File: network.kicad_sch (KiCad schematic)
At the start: 65 parts, among them J1 1840888-1, Q1 BSS138, Q2 BSS138, Q3 BSS138, U2 DP83867IRPAPR, Y1 ECS-2520MV-xxx-xx

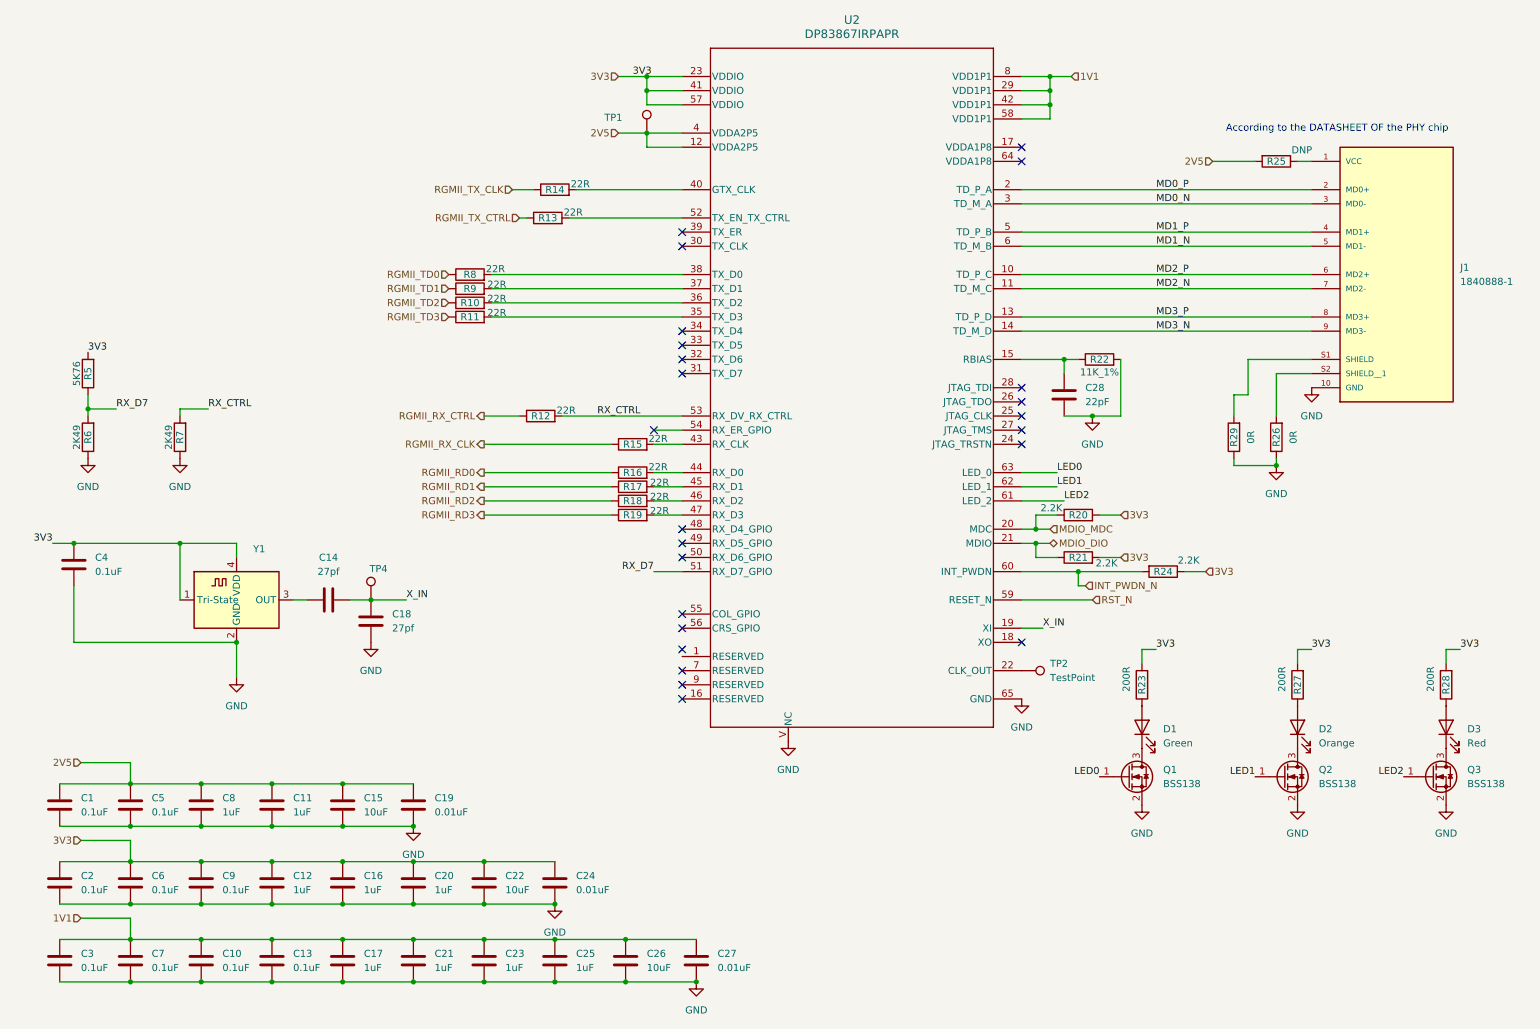
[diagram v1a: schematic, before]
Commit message: Nest network into phy, rj45_connector_port0 and oscillator sheets
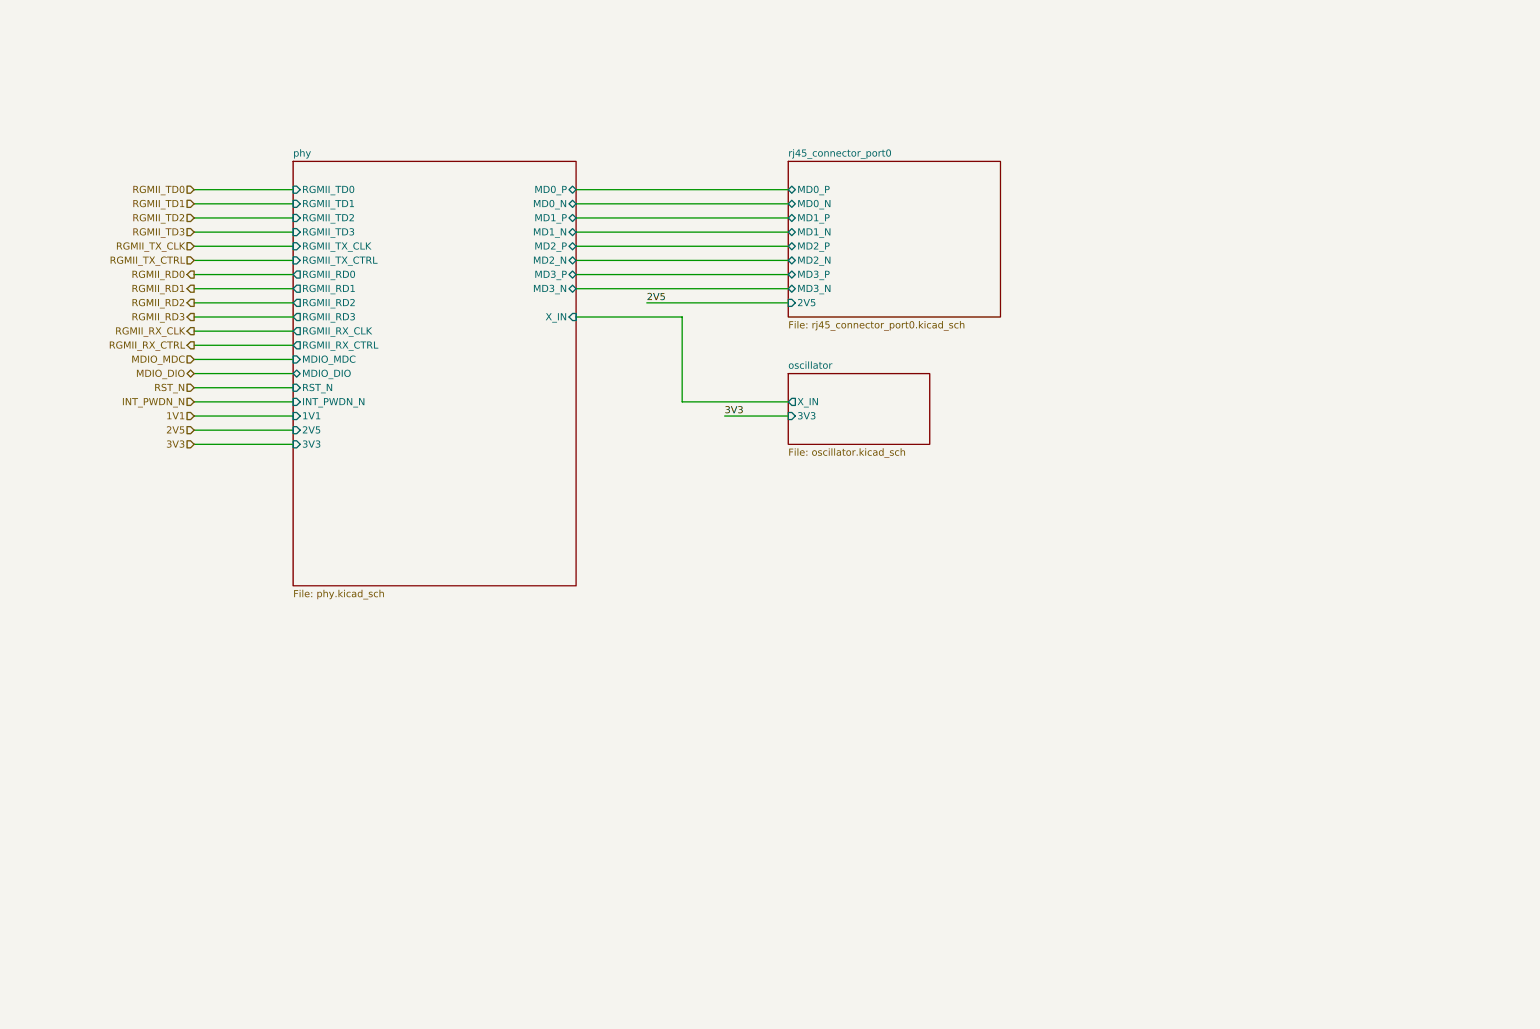
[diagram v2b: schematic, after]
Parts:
- removed C1, C10, C13, C2, C3, C4, C5, C6, C7, C9: 0.1uF, Capacitor_SMD:C_0402_1005Metric_Pad0.74x0.62mm_HandSolder, symbol Device:C
- removed C11, C12, C16, C17, C20, C21, C23, C25, C8: 1uF, Capacitor_SMD:C_0402_1005Metric_Pad0.74x0.62mm_HandSolder, symbol Device:C
- removed C14, C18: 27pf, Capacitor_SMD:C_0402_1005Metric_Pad0.74x0.62mm_HandSolder, symbol Device:C
- removed C15, C22, C26: 10uF, Capacitor_SMD:C_0402_1005Metric_Pad0.74x0.62mm_HandSolder, symbol Device:C
- removed C19, C24, C27: 0.01uF, Capacitor_SMD:C_0402_1005Metric_Pad0.74x0.62mm_HandSolder, symbol Device:C
- removed C28: 22pF, Capacitor_SMD:C_0402_1005Metric_Pad0.74x0.62mm_HandSolder, symbol Device:C
- removed D1: Green, LED_SMD:LED_0805_2012Metric, symbol Device:LED
- removed D2: Orange, LED_SMD:LED_0805_2012Metric, symbol Device:LED
- removed D3: Red, LED_SMD:LED_0805_2012Metric, symbol Device:LED
- removed J1: 1840888-1, 1840888_1:BEL_1840888-1, symbol 1840888-1:1840888-1
- removed Q1, Q2, Q3: BSS138, Package_TO_SOT_SMD:SOT-23, symbol Transistor_FET:BSS138
- removed R10, R11, R12, R13, R14, R15, R16, R17, R18, R19, R8, R9: 22R, Resistor_SMD:R_0402_1005Metric_Pad0.72x0.64mm_HandSolder, symbol Device:R
- removed R20, R21, R24: 2.2K, Resistor_SMD:R_0402_1005Metric_Pad0.72x0.64mm_HandSolder, symbol Device:R
- removed R22: 11K_1%, Resistor_SMD:R_0402_1005Metric_Pad0.72x0.64mm_HandSolder, symbol Device:R
- removed R23, R27, R28: 200R, Resistor_SMD:R_0402_1005Metric_Pad0.72x0.64mm_HandSolder, symbol Device:R
- removed R25: DNP, Resistor_SMD:R_0402_1005Metric_Pad0.72x0.64mm_HandSolder, symbol Device:R
- removed R26, R29: 0R, Resistor_SMD:R_0402_1005Metric_Pad0.72x0.64mm_HandSolder, symbol Device:R
- removed R5: 5K76, Resistor_SMD:R_0402_1005Metric_Pad0.72x0.64mm_HandSolder, symbol Device:R
- removed R6, R7: 2K49, Resistor_SMD:R_0402_1005Metric_Pad0.72x0.64mm_HandSolder, symbol Device:R
- removed TP1, TP2, TP4: TestPoint, TestPoint:TestPoint_Pad_1.0x1.0mm, symbol Connector:TestPoint
- removed U2: DP83867IRPAPR, PAP0064M_N, symbol DP83867:DP83867IRPAPR
- removed Y1: ECS-2520MV-xxx-xx, Oscillator:Oscillator_SMD_ECS_2520MV-xxx-xx-4Pin_2.5x2.0mm, symbol Oscillator:ECS-2520MV-xxx-xx
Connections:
- no-connect marks 24 -> 0
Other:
- added sheet oscillator (oscillator.kicad_sch)
- added sheet phy (phy.kicad_sch)
- added sheet rj45_connector_port0 (rj45_connector_port0.kicad_sch)
- note removed: "According to the DATASHEET OF the PHY chip"
- company: Kebag Logic: kebag-logic.com -> (none)

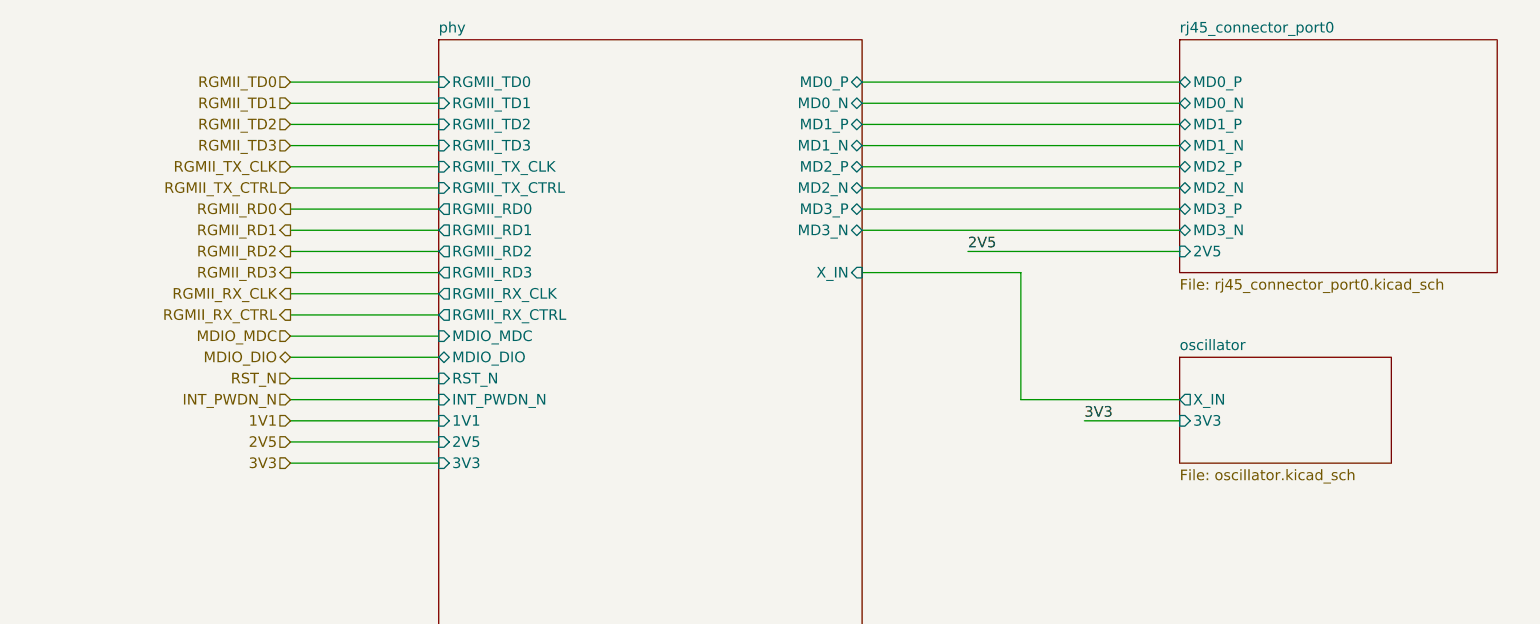
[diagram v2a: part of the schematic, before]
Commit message: Apply signal naming convention to all nets
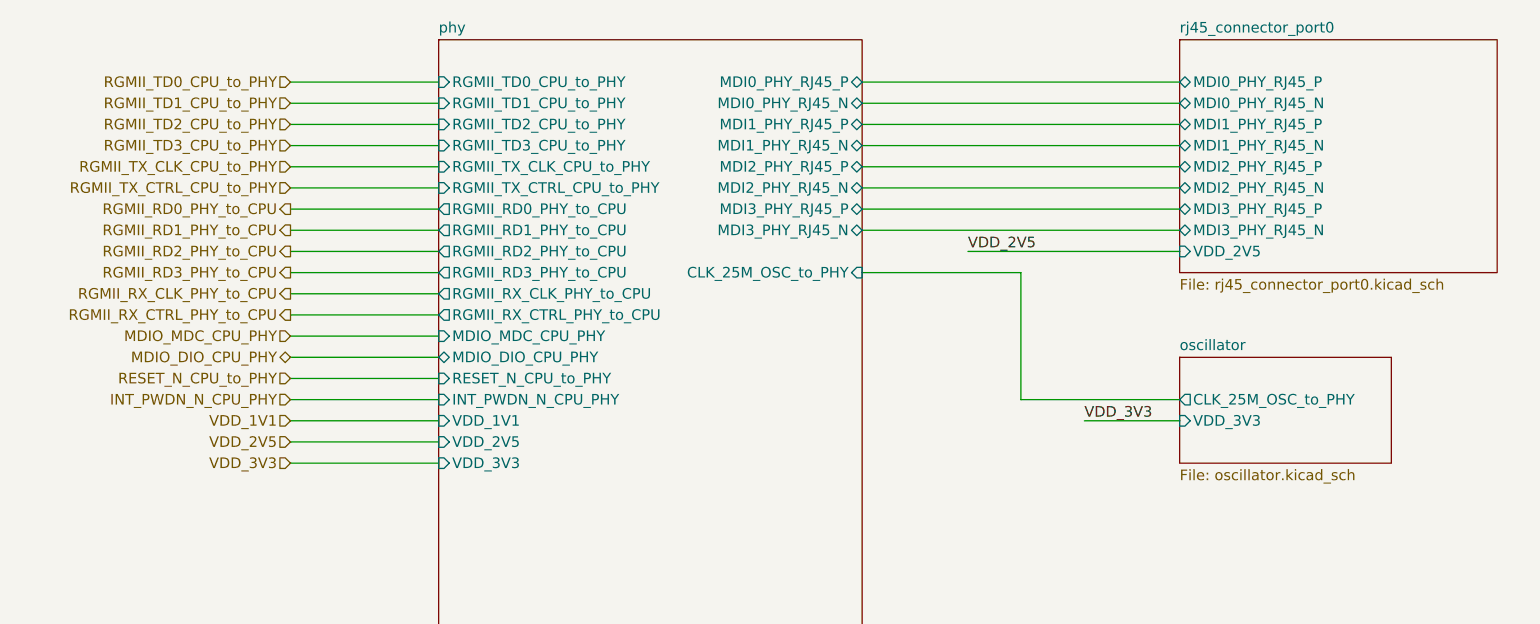
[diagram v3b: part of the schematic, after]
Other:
- sheet oscillator ports: added CLK_25M_OSC_to_PHY, VDD_3V3; removed 3V3, X_IN
- sheet phy ports: added CLK_25M_OSC_to_PHY, INT_PWDN_N_CPU_PHY, MDI0_PHY_RJ45_N, MDI0_PHY_RJ45_P, MDI1_PHY_RJ45_N, MDI1_PHY_RJ45_P, MDI2_PHY_RJ45_N, MDI2_PHY_RJ45_P, MDI3_PHY_RJ45_N, MDI3_PHY_RJ45_P, MDIO_DIO_CPU_PHY, MDIO_MDC_CPU_PHY, RESET_N_CPU_to_PHY, RGMII_RD0_PHY_to_CPU, RGMII_RD1_PHY_to_CPU, RGMII_RD2_PHY_to_CPU, RGMII_RD3_PHY_to_CPU, RGMII_RX_CLK_PHY_to_CPU, RGMII_RX_CTRL_PHY_to_CPU, RGMII_TD0_CPU_to_PHY, RGMII_TD1_CPU_to_PHY, RGMII_TD2_CPU_to_PHY, RGMII_TD3_CPU_to_PHY, RGMII_TX_CLK_CPU_to_PHY, RGMII_TX_CTRL_CPU_to_PHY, VDD_1V1, VDD_2V5, VDD_3V3; removed 1V1, 2V5, 3V3, INT_PWDN_N, MD0_N, MD0_P, MD1_N, MD1_P, MD2_N, MD2_P, MD3_N, MD3_P, MDIO_DIO, MDIO_MDC, RGMII_RD0, RGMII_RD1, RGMII_RD2, RGMII_RD3, RGMII_RX_CLK, RGMII_RX_CTRL, RGMII_TD0, RGMII_TD1, RGMII_TD2, RGMII_TD3, RGMII_TX_CLK, RGMII_TX_CTRL, RST_N, X_IN
- sheet rj45_connector_port0 ports: added MDI0_PHY_RJ45_N, MDI0_PHY_RJ45_P, MDI1_PHY_RJ45_N, MDI1_PHY_RJ45_P, MDI2_PHY_RJ45_N, MDI2_PHY_RJ45_P, MDI3_PHY_RJ45_N, MDI3_PHY_RJ45_P, VDD_2V5; removed 2V5, MD0_N, MD0_P, MD1_N, MD1_P, MD2_N, MD2_P, MD3_N, MD3_P
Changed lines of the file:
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@@
 			)
 		)
-		(pin "RGMII_TD0" input
+		(pin "RGMII_TD0_CPU_to_PHY" input
 			(at 63.5 43.18 180)
 			(effects
@@
 			)
 		)
-		(pin "RGMII_TD1" input
+		(pin "RGMII_TD1_CPU_to_PHY" input
 			(at 63.5 45.72 180)
 			(effects
@@
 			)
 		)
-		(pin "RGMII_TD2" input
+		(pin "RGMII_TD2_CPU_to_PHY" input
 			(at 63.5 48.26 180)
 			(effects
@@
 			)
 		)
-		(pin "RGMII_TD3" input
+		(pin "RGMII_TD3_CPU_to_PHY" input
 			(at 63.5 50.8 180)
 			(effects
@@
 			)
 		)
-		(pin "RGMII_TX_CLK" input
+		(pin "RGMII_TX_CLK_CPU_to_PHY" input
 			(at 63.5 53.34 180)
 			(effects
@@
 			)
 		)
-		(pin "RGMII_TX_CTRL" input
+		(pin "RGMII_TX_CTRL_CPU_to_PHY" input
 			(at 63.5 55.88 180)
 			(effects
@@
 			)
 		)
-		(pin "RGMII_RD0" output
+		(pin "RGMII_RD0_PHY_to_CPU" output
 			(at 63.5 58.42 180)
 			(effects
@@
 			)
 		)
-		(pin "RGMII_RD1" output
+		(pin "RGMII_RD1_PHY_to_CPU" output
 			(at 63.5 60.96 180)
 			(effects
@@
 			)
 		)
-		(pin "RGMII_RD2" output
+		(pin "RGMII_RD2_PHY_to_CPU" output
 			(at 63.5 63.5 180)
 			(effects
@@
 			)
 		)
-		(pin "RGMII_RD3" output
+		(pin "RGMII_RD3_PHY_to_CPU" output
 			(at 63.5 66.04 180)
 			(effects
@@
 			)
 		)
-		(pin "RGMII_RX_CLK" output
+		(pin "RGMII_RX_CLK_PHY_to_CPU" output
 			(at 63.5 68.58 180)
 			(effects
@@
 			)
 		)
-		(pin "RGMII_RX_CTRL" output
+		(pin "RGMII_RX_CTRL_PHY_to_CPU" output
 			(at 63.5 71.12 180)
 			(effects
@@
 			)
 		)
-		(pin "MDIO_MDC" input
+		(pin "MDIO_MDC_CPU_PHY" input
 			(at 63.5 73.66 180)
 			(effects
@@
 			)
 		)
-		(pin "MDIO_DIO" bidirectional
+		(pin "MDIO_DIO_CPU_PHY" bidirectional
 			(at 63.5 76.2 180)
 			(effects
@@
 			)
 		)
-		(pin "RST_N" input
+		(pin "RESET_N_CPU_to_PHY" input
 			(at 63.5 78.74 180)
 			(effects
@@
 			)
 		)
-		(pin "INT_PWDN_N" input
+		(pin "INT_PWDN_N_CPU_PHY" input
 			(at 63.5 81.28 180)
 			(effects
@@
 			)
 		)
-		(pin "1V1" input
+		(pin "VDD_1V1" input
 			(at 63.5 83.82 180)
 			(effects
@@
 			)
 		)
-		(pin "2V5" input
+		(pin "VDD_2V5" input
 			(at 63.5 86.36 180)
 			(effects
@@
 			)
 		)
-		(pin "3V3" input
+		(pin "VDD_3V3" input
 			(at 63.5 88.9 180)
 			(effects
@@
 			)
 		)
-		(pin "MD0_P" bidirectional
+		(pin "MDI0_PHY_RJ45_P" bidirectional
 			(at 114.3 43.18 0)
 			(effects
@@
 			)
 		)
-		(pin "MD0_N" bidirectional
+		(pin "MDI0_PHY_RJ45_N" bidirectional
 			(at 114.3 45.72 0)
 			(effects
@@
 			)
 		)
-		(pin "MD1_P" bidirectional
+		(pin "MDI1_PHY_RJ45_P" bidirectional
 			(at 114.3 48.26 0)
 			(effects
@@
 			)
 		)
-		(pin "MD1_N" bidirectional
+		(pin "MDI1_PHY_RJ45_N" bidirectional
 			(at 114.3 50.8 0)
 			(effects
@@
 			)
 		)
-		(pin "MD2_P" bidirectional
+		(pin "MDI2_PHY_RJ45_P" bidirectional
 			(at 114.3 53.34 0)
 			(effects
@@
 			)
 		)
-		(pin "MD2_N" bidirectional
+		(pin "MDI2_PHY_RJ45_N" bidirectional
 			(at 114.3 55.88 0)
 			(effects
@@
 			)
 		)
-		(pin "MD3_P" bidirectional
+		(pin "MDI3_PHY_RJ45_P" bidirectional
 			(at 114.3 58.42 0)
 			(effects
@@
 			)
 		)
-		(pin "MD3_N" bidirectional
+		(pin "MDI3_PHY_RJ45_N" bidirectional
 			(at 114.3 60.96 0)
 			(effects
@@
 			)
 		)
-		(pin "X_IN" input
+		(pin "CLK_25M_OSC_to_PHY" input
 			(at 114.3 66.04 0)
 			(effects
@@
 			)
 		)
-		(pin "MD0_P" bidirectional
+		(pin "MDI0_PHY_RJ45_P" bidirectional
 			(at 152.4 43.18 180)
 			(effects
@@
 			)
 		)
-		(pin "MD0_N" bidirectional
+		(pin "MDI0_PHY_RJ45_N" bidirectional
 			(at 152.4 45.72 180)
 			(effects
@@
 			)
 		)
-		(pin "MD1_P" bidirectional
+		(pin "MDI1_PHY_RJ45_P" bidirectional
 			(at 152.4 48.26 180)
 			(effects
@@
 			)
 		)
-		(pin "MD1_N" bidirectional
+		(pin "MDI1_PHY_RJ45_N" bidirectional
 			(at 152.4 50.8 180)
 			(effects
@@
 			)
 		)
-		(pin "MD2_P" bidirectional
+		(pin "MDI2_PHY_RJ45_P" bidirectional
 			(at 152.4 53.34 180)
 			(effects
@@
 			)
 		)
-		(pin "MD2_N" bidirectional
+		(pin "MDI2_PHY_RJ45_N" bidirectional
 			(at 152.4 55.88 180)
 			(effects
@@
 			)
 		)
-		(pin "MD3_P" bidirectional
+		(pin "MDI3_PHY_RJ45_P" bidirectional
 			(at 152.4 58.42 180)
 			(effects
@@
 			)
 		)
-		(pin "MD3_N" bidirectional
+		(pin "MDI3_PHY_RJ45_N" bidirectional
 			(at 152.4 60.96 180)
 			(effects
@@
 			)
 		)
-		(pin "2V5" input
+		(pin "VDD_2V5" input
 			(at 152.4 63.5 180)
 			(effects
@@
 			)
 		)
-		(pin "X_IN" output
+		(pin "CLK_25M_OSC_to_PHY" output
 			(at 152.4 81.28 180)
 			(effects
@@
 			)
 		)
-		(pin "3V3" input
+		(pin "VDD_3V3" input
 			(at 152.4 83.82 180)
 			(effects
@@
 		)
 	)
-	(hierarchical_label "RGMII_TD0"
+	(hierarchical_label "RGMII_TD0_CPU_to_PHY"
 		(shape input)
 		(at 45.72 43.18 180)
@@
 		)
 	)
-	(hierarchical_label "RGMII_TD1"
+	(hierarchical_label "RGMII_TD1_CPU_to_PHY"
 		(shape input)
 		(at 45.72 45.72 180)
@@
 		)
 	)
-	(hierarchical_label "RGMII_TD2"
+	(hierarchical_label "RGMII_TD2_CPU_to_PHY"
 		(shape input)
 		(at 45.72 48.26 180)
@@
 		)
 	)
-	(hierarchical_label "RGMII_TD3"
+	(hierarchical_label "RGMII_TD3_CPU_to_PHY"
 		(shape input)
 		(at 45.72 50.8 180)
@@
 		)
 	)
-	(hierarchical_label "RGMII_TX_CLK"
+	(hierarchical_label "RGMII_TX_CLK_CPU_to_PHY"
 		(shape input)
 		(at 45.72 53.34 180)
@@
 		)
 	)
-	(hierarchical_label "RGMII_TX_CTRL"
+	(hierarchical_label "RGMII_TX_CTRL_CPU_to_PHY"
 		(shape input)
 		(at 45.72 55.88 180)
@@
 		)
 	)
-	(hierarchical_label "RGMII_RD0"
+	(hierarchical_label "RGMII_RD0_PHY_to_CPU"
 		(shape output)
 		(at 45.72 58.42 180)
@@
 		)
 	)
-	(hierarchical_label "RGMII_RD1"
+	(hierarchical_label "RGMII_RD1_PHY_to_CPU"
 		(shape output)
 		(at 45.72 60.96 180)
@@
 		)
 	)
-	(hierarchical_label "RGMII_RD2"
+	(hierarchical_label "RGMII_RD2_PHY_to_CPU"
 		(shape output)
 		(at 45.72 63.5 180)
@@
 		)
 	)
-	(hierarchical_label "RGMII_RD3"
+	(hierarchical_label "RGMII_RD3_PHY_to_CPU"
 		(shape output)
 		(at 45.72 66.04 180)
@@
 		)
 	)
-	(hierarchical_label "RGMII_RX_CLK"
+	(hierarchical_label "RGMII_RX_CLK_PHY_to_CPU"
 		(shape output)
 		(at 45.72 68.58 180)
@@
 		)
 	)
-	(hierarchical_label "RGMII_RX_CTRL"
+	(hierarchical_label "RGMII_RX_CTRL_PHY_to_CPU"
 		(shape output)
 		(at 45.72 71.12 180)
@@
 		)
 	)
-	(hierarchical_label "MDIO_MDC"
+	(hierarchical_label "MDIO_MDC_CPU_PHY"
 		(shape input)
 		(at 45.72 73.66 180)
@@
 		)
 	)
-	(hierarchical_label "MDIO_DIO"
+	(hierarchical_label "MDIO_DIO_CPU_PHY"
 		(shape bidirectional)
 		(at 45.72 76.2 180)
@@
 		)
 	)
-	(hierarchical_label "RST_N"
+	(hierarchical_label "RESET_N_CPU_to_PHY"
 		(shape input)
 		(at 45.72 78.74 180)
@@
 		)
 	)
-	(hierarchical_label "INT_PWDN_N"
+	(hierarchical_label "INT_PWDN_N_CPU_PHY"
 		(shape input)
 		(at 45.72 81.28 180)
@@
 		)
 	)
-	(hierarchical_label "1V1"
+	(hierarchical_label "VDD_1V1"
 		(shape input)
 		(at 45.72 83.82 180)
@@
 		)
 	)
-	(hierarchical_label "2V5"
+	(hierarchical_label "VDD_2V5"
 		(shape input)
 		(at 45.72 86.36 180)
@@
 		)
 	)
-	(hierarchical_label "3V3"
+	(hierarchical_label "VDD_3V3"
 		(shape input)
 		(at 45.72 88.9 180)
@@
 		)
 	)
-	(label "2V5"
+	(label "VDD_2V5"
 		(at 127.0 63.5 0)
 		(effects
@@
 		)
 	)
-	(label "3V3"
+	(label "VDD_3V3"
 		(at 140.97 83.82 0)
 		(effects
